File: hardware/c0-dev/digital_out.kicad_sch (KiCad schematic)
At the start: 17 parts, among them U33 B0505S-1WR3, U34 ISO1540, U35 TCA9555PWR

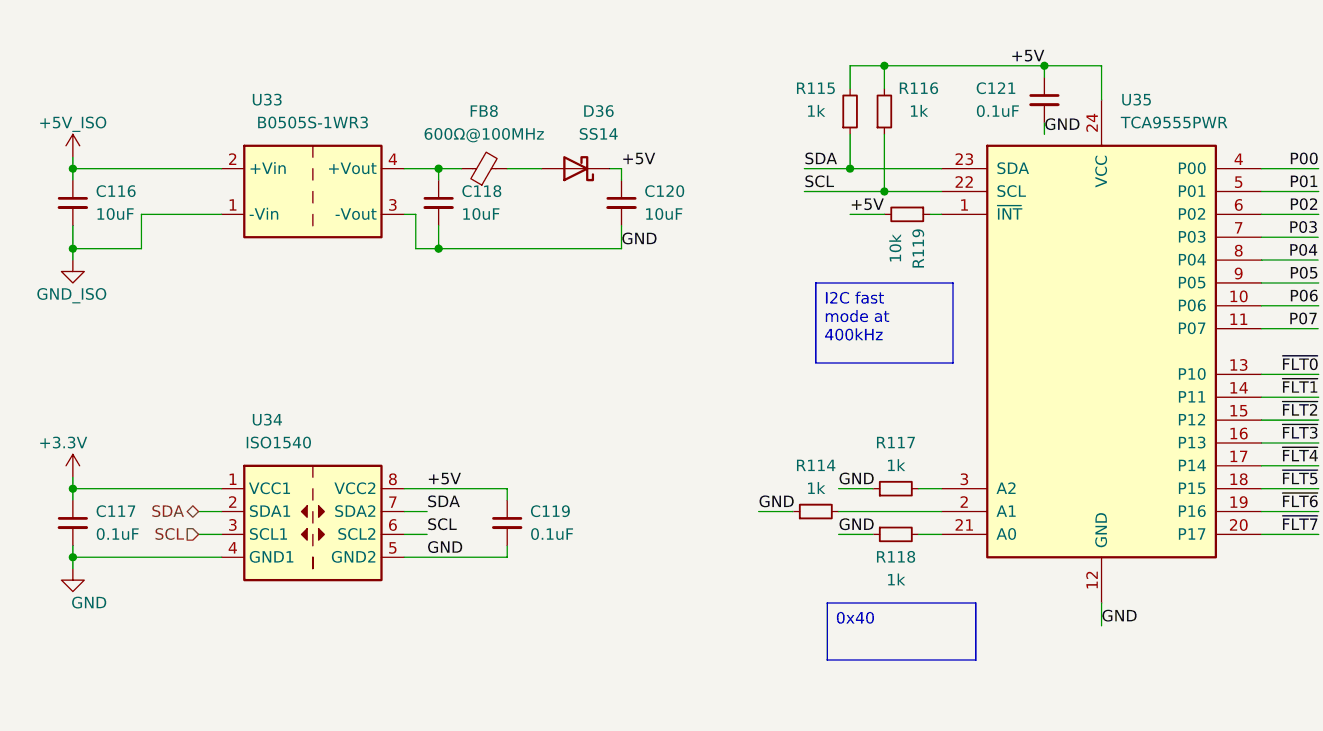
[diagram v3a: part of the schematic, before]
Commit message: added connectors
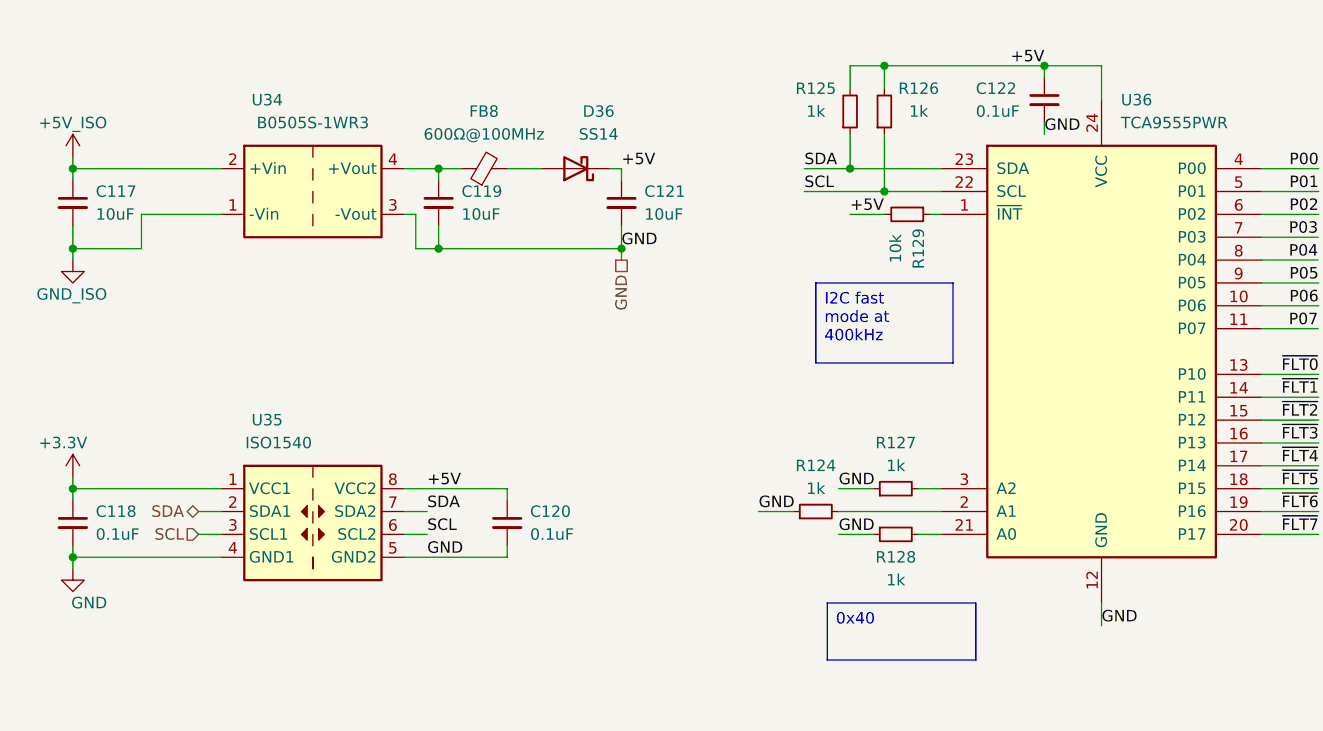
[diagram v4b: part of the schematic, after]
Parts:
- renumbered C116 to C117, C117 to C118, C118 to C119, C119 to C120, C120 to C121, C121 to C122, R114 to R124, R115 to R125, R116 to R126, R117 to R127, R118 to R128, R119 to R129, U33 to U34, U34 to U35, U35 to U36
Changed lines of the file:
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@@
 	)
 	(junction
+		(at 97.79 44.45)
+		(diameter 0)
+		(color 0 0 0 0)
+	)
+	(junction
 		(at 77.47 35.56)
 		(diameter 0)
@@
 	(wire
 		(pts
+			(xy 97.79 44.45) (xy 97.79 45.72)
+		)
+		(stroke
+			(width 0)
+			(type default)
+		)
+	)
+	(wire
+		(pts
 			(xy 121.92 76.2) (xy 125.73 76.2)
 		)
@@
 		)
 	)
+	(hierarchical_label "GND"
+		(shape passive)
+		(at 97.79 45.72 270)
+		(effects
+			(font
+				(size 1.27 1.27)
+			)
+			(justify right)
+		)
+	)
 	(hierarchical_label "OUT3"
 		(shape output)
@@
 		(in_pos_files yes)
 		(dnp no)
-		(property "Reference" "R117"
+		(property "Reference" "R127"
 			(at 128.27 66.04 90)
 			(show_name no)
@@
 			(project "c0-dev"
 				(path "/b8347a0e-ad04-4414-969d-3c64a611d74e/680032e3-5da4-48ad-9c49-e468cbbeffb9"
-					(reference "R117")
+					(reference "R127")
 					(unit 1)
 				)
@@
 		(in_pos_files yes)
 		(dnp no)
-		(property "Reference" "R119"
+		(property "Reference" "R129"
 			(at 130.81 44.45 0)
 			(show_name no)
@@
 			(project "c0-dev"
 				(path "/b8347a0e-ad04-4414-969d-3c64a611d74e/680032e3-5da4-48ad-9c49-e468cbbeffb9"
-					(reference "R119")
+					(reference "R129")
 					(unit 1)
 				)
@@
 		(in_pos_files yes)
 		(dnp no)
-		(property "Reference" "#PWR090"
+		(property "Reference" "#PWR0128"
 			(at 36.83 73.66 0)
 			(hide yes)
@@
 			(project "c0-dev"
 				(path "/b8347a0e-ad04-4414-969d-3c64a611d74e/680032e3-5da4-48ad-9c49-e468cbbeffb9"
-					(reference "#PWR090")
+					(reference "#PWR0128")
 					(unit 1)
 				)
@@
 		(in_pos_files yes)
 		(dnp no)
-		(property "Reference" "U34"
+		(property "Reference" "U35"
 			(at 58.42 63.5 0)
 			(show_name no)
@@
 			(project "c0-dev"
 				(path "/b8347a0e-ad04-4414-969d-3c64a611d74e/680032e3-5da4-48ad-9c49-e468cbbeffb9"
-					(reference "U34")
+					(reference "U35")
 					(unit 1)
 				)
@@
 		(dnp no)
 		(fields_autoplaced yes)
-		(property "Reference" "C116"
+		(property "Reference" "C117"
 			(at 39.37 38.1062 0)
 			(show_name no)
@@
 			(project "c0-dev"
 				(path "/b8347a0e-ad04-4414-969d-3c64a611d74e/680032e3-5da4-48ad-9c49-e468cbbeffb9"
-					(reference "C116")
+					(reference "C117")
 					(unit 1)
 				)
@@
 		(in_pos_files yes)
 		(dnp no)
-		(property "Reference" "R116"
+		(property "Reference" "R126"
 			(at 130.81 26.67 0)
 			(show_name no)
@@
 			(project "c0-dev"
 				(path "/b8347a0e-ad04-4414-969d-3c64a611d74e/680032e3-5da4-48ad-9c49-e468cbbeffb9"
-					(reference "R116")
+					(reference "R126")
 					(unit 1)
 				)
@@
 		(in_pos_files yes)
 		(dnp no)
-		(property "Reference" "#PWR086"
+		(property "Reference" "#PWR0127"
 			(at 36.83 52.07 0)
 			(hide yes)
@@
 			(project "c0-dev"
 				(path "/b8347a0e-ad04-4414-969d-3c64a611d74e/680032e3-5da4-48ad-9c49-e468cbbeffb9"
-					(reference "#PWR086")
+					(reference "#PWR0127")
 					(unit 1)
 				)
@@
 		(in_pos_files yes)
 		(dnp no)
-		(property "Reference" "R118"
+		(property "Reference" "R128"
 			(at 128.27 78.74 90)
 			(show_name no)
@@
 			(project "c0-dev"
 				(path "/b8347a0e-ad04-4414-969d-3c64a611d74e/680032e3-5da4-48ad-9c49-e468cbbeffb9"
-					(reference "R118")
+					(reference "R128")
 					(unit 1)
 				)
@@
 		(in_pos_files yes)
 		(dnp no)
-		(property "Reference" "#PWR091"
+		(property "Reference" "#PWR0129"
 			(at 36.83 86.36 0)
 			(hide yes)
@@
 			(project "c0-dev"
 				(path "/b8347a0e-ad04-4414-969d-3c64a611d74e/680032e3-5da4-48ad-9c49-e468cbbeffb9"
-					(reference "#PWR091")
+					(reference "#PWR0129")
 					(unit 1)
 				)
@@
 		(dnp no)
 		(fields_autoplaced yes)
-		(property "Reference" "C120"
+		(property "Reference" "C121"
 			(at 100.33 38.1062 0)
 			(show_name no)
@@
 			(project "c0-dev"
 				(path "/b8347a0e-ad04-4414-969d-3c64a611d74e/680032e3-5da4-48ad-9c49-e468cbbeffb9"
-					(reference "C120")
+					(reference "C121")
 					(unit 1)
 				)
@@
 		(dnp no)
 		(fields_autoplaced yes)
-		(property "Reference" "C117"
+		(property "Reference" "C118"
 			(at 39.37 73.6662 0)
 			(show_name no)
@@
 			(project "c0-dev"
 				(path "/b8347a0e-ad04-4414-969d-3c64a611d74e/680032e3-5da4-48ad-9c49-e468cbbeffb9"
-					(reference "C117")
+					(reference "C118")
 					(unit 1)
 				)
@@
 		(dnp no)
 		(fields_autoplaced yes)
-		(property "Reference" "C119"
+		(property "Reference" "C120"
 			(at 87.63 73.6662 0)
 			(show_name no)
@@
 			(project "c0-dev"
 				(path "/b8347a0e-ad04-4414-969d-3c64a611d74e/680032e3-5da4-48ad-9c49-e468cbbeffb9"
-					(reference "C119")
+					(reference "C120")
 					(unit 1)
 				)
@@
 		(in_pos_files yes)
 		(dnp no)
-		(property "Reference" "U33"
+		(property "Reference" "U34"
 			(at 58.42 27.94 0)
 			(show_name no)
@@
 			(project "c0-dev"
 				(path "/b8347a0e-ad04-4414-969d-3c64a611d74e/680032e3-5da4-48ad-9c49-e468cbbeffb9"
-					(reference "U33")
+					(reference "U34")
 					(unit 1)
 				)
@@
 		(in_pos_files yes)
 		(dnp no)
-		(property "Reference" "R114"
+		(property "Reference" "R124"
 			(at 119.38 68.58 90)
 			(show_name no)
@@
 			(project "c0-dev"
 				(path "/b8347a0e-ad04-4414-969d-3c64a611d74e/680032e3-5da4-48ad-9c49-e468cbbeffb9"
-					(reference "R114")
+					(reference "R124")
 					(unit 1)
 				)
@@
 		(dnp no)
 		(fields_autoplaced yes)
-		(property "Reference" "C118"
+		(property "Reference" "C119"
 			(at 80.01 38.1062 0)
 			(show_name no)
@@
 			(project "c0-dev"
 				(path "/b8347a0e-ad04-4414-969d-3c64a611d74e/680032e3-5da4-48ad-9c49-e468cbbeffb9"
-					(reference "C118")
+					(reference "C119")
 					(unit 1)
 				)
@@
 		(dnp no)
 		(fields_autoplaced yes)
-		(property "Reference" "U35"
+		(property "Reference" "U36"
 			(at 153.2733 27.94 0)
 			(show_name no)
@@
 			(project "c0-dev"
 				(path "/b8347a0e-ad04-4414-969d-3c64a611d74e/680032e3-5da4-48ad-9c49-e468cbbeffb9"
-					(reference "U35")
+					(reference "U36")
 					(unit 1)
 				)
@@
 		(in_pos_files yes)
 		(dnp no)
-		(property "Reference" "R115"
+		(property "Reference" "R125"
 			(at 119.38 26.67 0)
 			(show_name no)
@@
 			(project "c0-dev"
 				(path "/b8347a0e-ad04-4414-969d-3c64a611d74e/680032e3-5da4-48ad-9c49-e468cbbeffb9"
-					(reference "R115")
+					(reference "R125")
 					(unit 1)
 				)
@@
 		(in_pos_files yes)
 		(dnp no)
-		(property "Reference" "#PWR085"
+		(property "Reference" "#PWR0126"
 			(at 36.83 38.1 0)
 			(hide yes)
@@
 			(project "c0-dev"
 				(path "/b8347a0e-ad04-4414-969d-3c64a611d74e/680032e3-5da4-48ad-9c49-e468cbbeffb9"
-					(reference "#PWR085")
+					(reference "#PWR0126")
 					(unit 1)
 				)
@@
 		(in_pos_files yes)
 		(dnp no)
-		(property "Reference" "C121"
+		(property "Reference" "C122"
 			(at 137.16 26.67 0)
 			(show_name no)
@@
 			(project "c0-dev"
 				(path "/b8347a0e-ad04-4414-969d-3c64a611d74e/680032e3-5da4-48ad-9c49-e468cbbeffb9"
-					(reference "C121")
+					(reference "C122")
 					(unit 1)
 				)

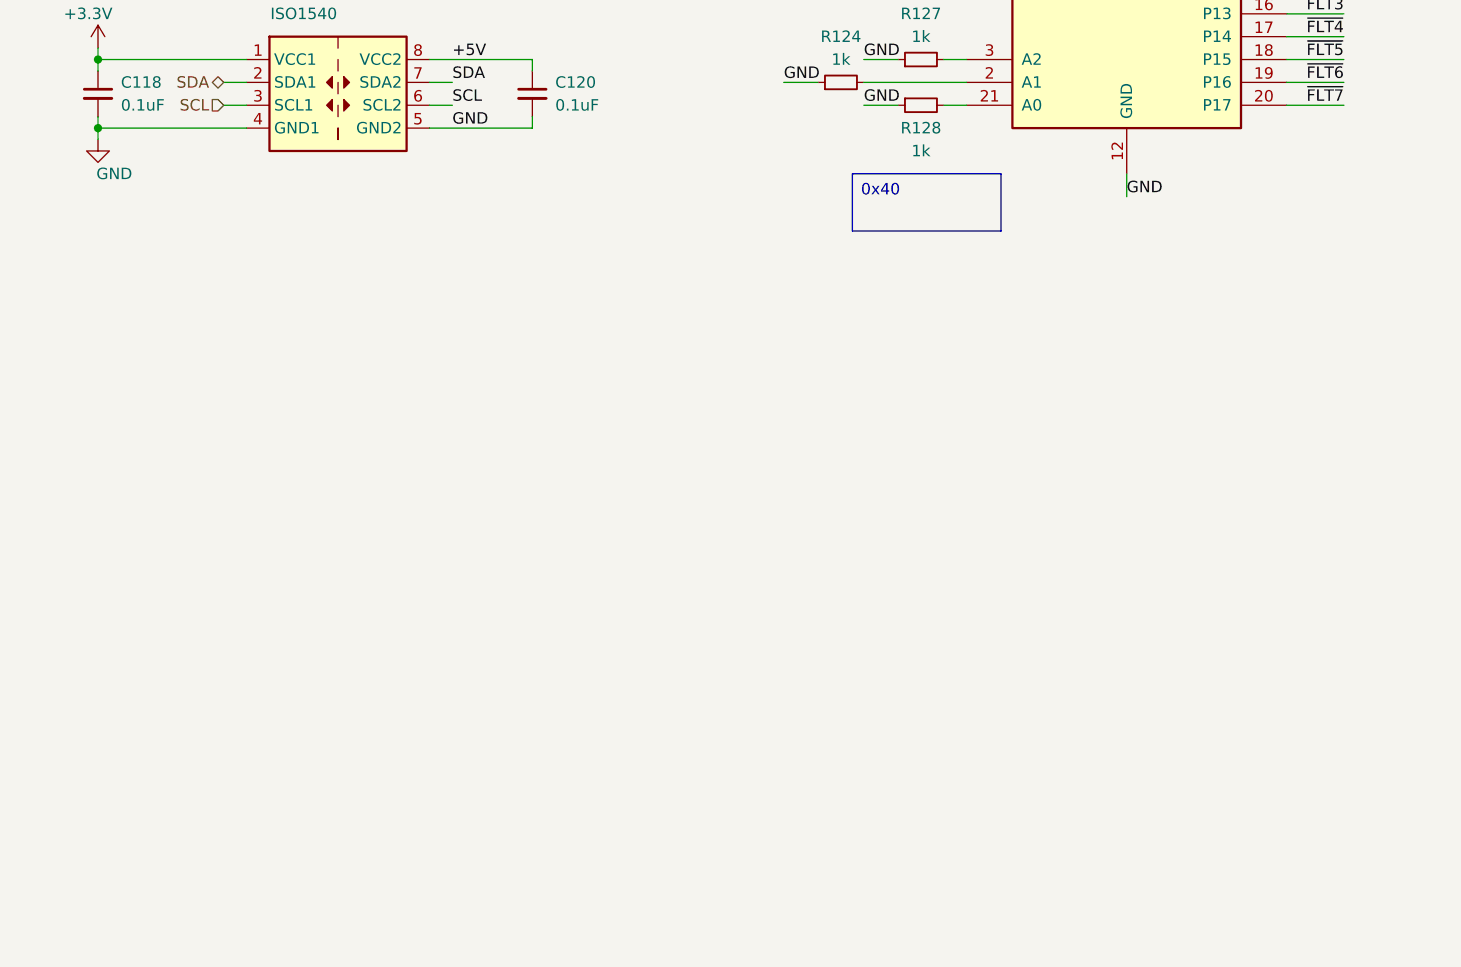
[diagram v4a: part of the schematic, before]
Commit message: added watchdog output disable
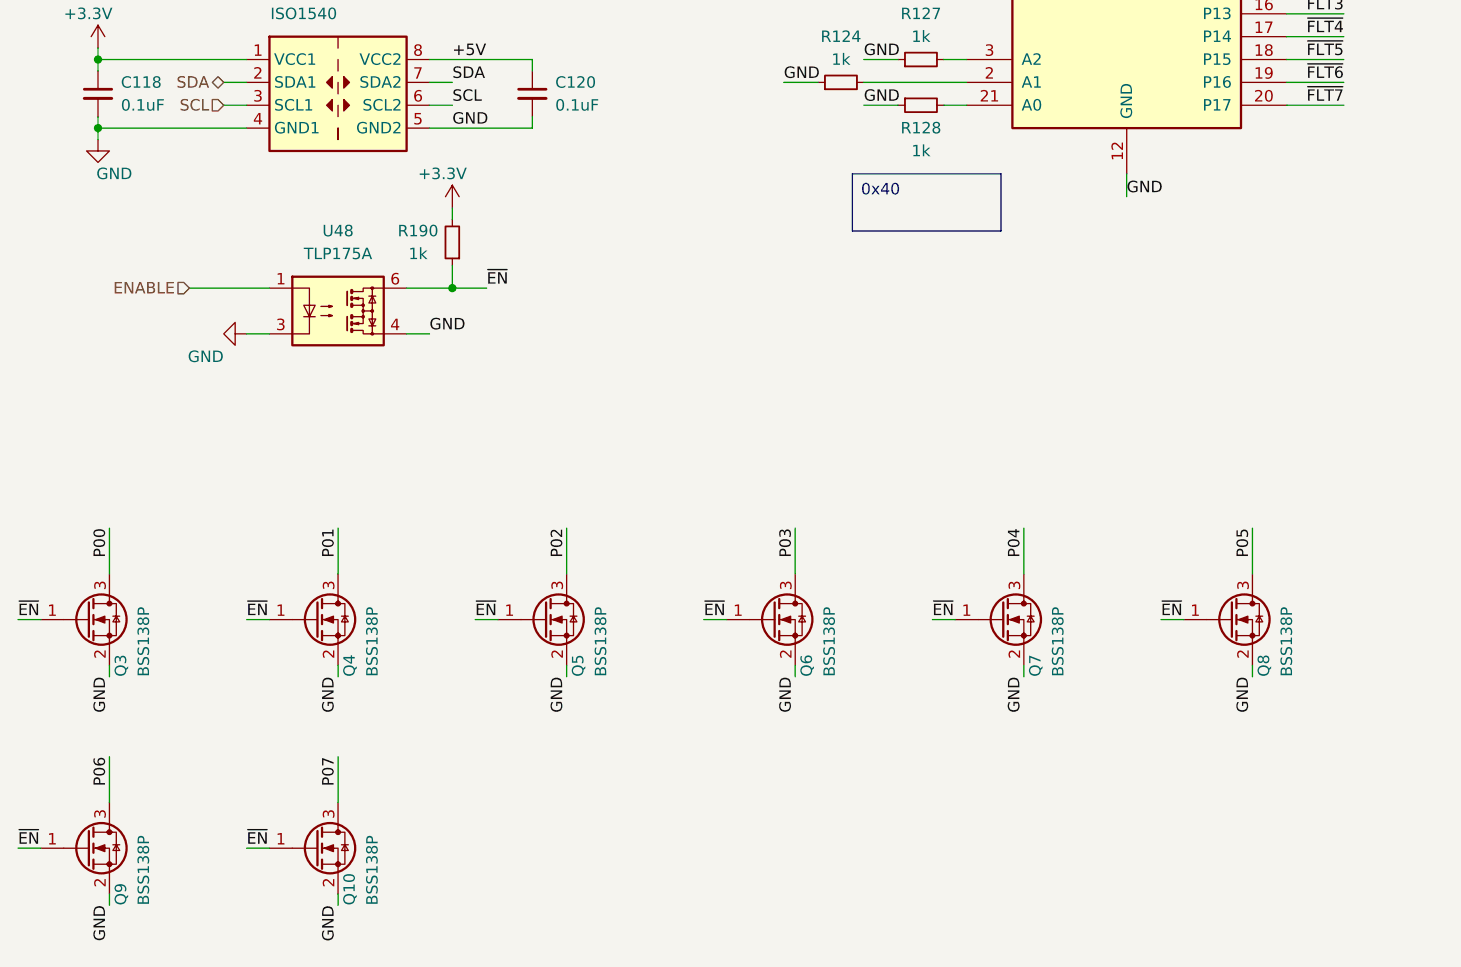
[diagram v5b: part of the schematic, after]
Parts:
- added Q10, Q3, Q4, Q5, Q6, Q7, Q8, Q9: BSS138P, Package_TO_SOT_SMD:SOT-23, symbol Transistor_FET:Q_NMOS_GSD
- added R190: 1k, Resistor_SMD:R_0402_1005Metric, symbol Device:R_Small
- added U48: TLP175A, Package_SO:Toshiba_SOIC-4-6_4.4x3.6mm_P1.27mm, symbol Relay_SolidState:TLP175A
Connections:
- net +3.3V: now also R190.2
- net GND: now also Q10.2 (S), Q3.2 (S), Q4.2 (S), Q5.2 (S), Q6.2 (S), Q7.2 (S), Q8.2 (S), Q9.2 (S), U48.3, U48.4
- net P00: now also Q3.3 (D)
- net P01: now also Q4.3 (D)
- net P02: now also Q5.3 (D)
- net P03: now also Q6.3 (D)
- net P04: now also Q7.3 (D)
- net P05: now also Q8.3 (D)
- net P06: now also Q9.3 (D)
- net P07: now also Q10.3 (D)
- new net ENABLE: U48.1
- new net ~{EN}: Q10.1 (G), Q3.1 (G), Q4.1 (G), Q5.1 (G), Q6.1 (G), Q7.1 (G), Q8.1 (G), Q9.1 (G), R190.1, U48.6
